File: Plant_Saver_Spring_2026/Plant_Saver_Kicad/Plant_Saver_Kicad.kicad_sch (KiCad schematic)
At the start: 21 parts, among them SW1 Up, SW2 Down, SW3 Change Screen, SW4 Select, U1 TPB4056A20-ES1R, U3 AMS1117-3.3, U5 ESP32-WROOM-32D

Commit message: Added Charging Schematic
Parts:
- added CR2, CR3, CR4: PMEG3050EP_115, SDO_CFP5_SOD128_NEX, symbol PMEG3050EP,115:PMEG3050EP_115
- added SC1, SC2, SC3: Solar_Cell, symbol Device:Solar_Cell
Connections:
- net GND: now also SC1.2 (-), SC2.2 (-), SC3.2 (-)
- new net Power_And_Charging/Solar: CR2.1, CR3.1, CR4.1
- new net Solar_Measurement1/Vin: CR2.2, SC1.1 (+)
- new net Solar_Measurement2/Vin: CR3.2, SC2.1 (+)
- new net Solar_Measurement3/Vin: CR4.2, SC3.1 (+)
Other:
- added sheet Power_And_Charging (Charge_Circuit.kicad_sch)
- added sheet Solar_Measurement1 (Solar_Measurement_Unit.kicad_sch)
- added sheet Solar_Measurement2 (Solar_Measurement_Unit.kicad_sch)
- added sheet Solar_Measurement3 (Solar_Measurement_Unit.kicad_sch)
- added sheet USB-C (USB_C.kicad_sch)
- moved on the sheet: SW1, SW2, SW3, SW4, U5

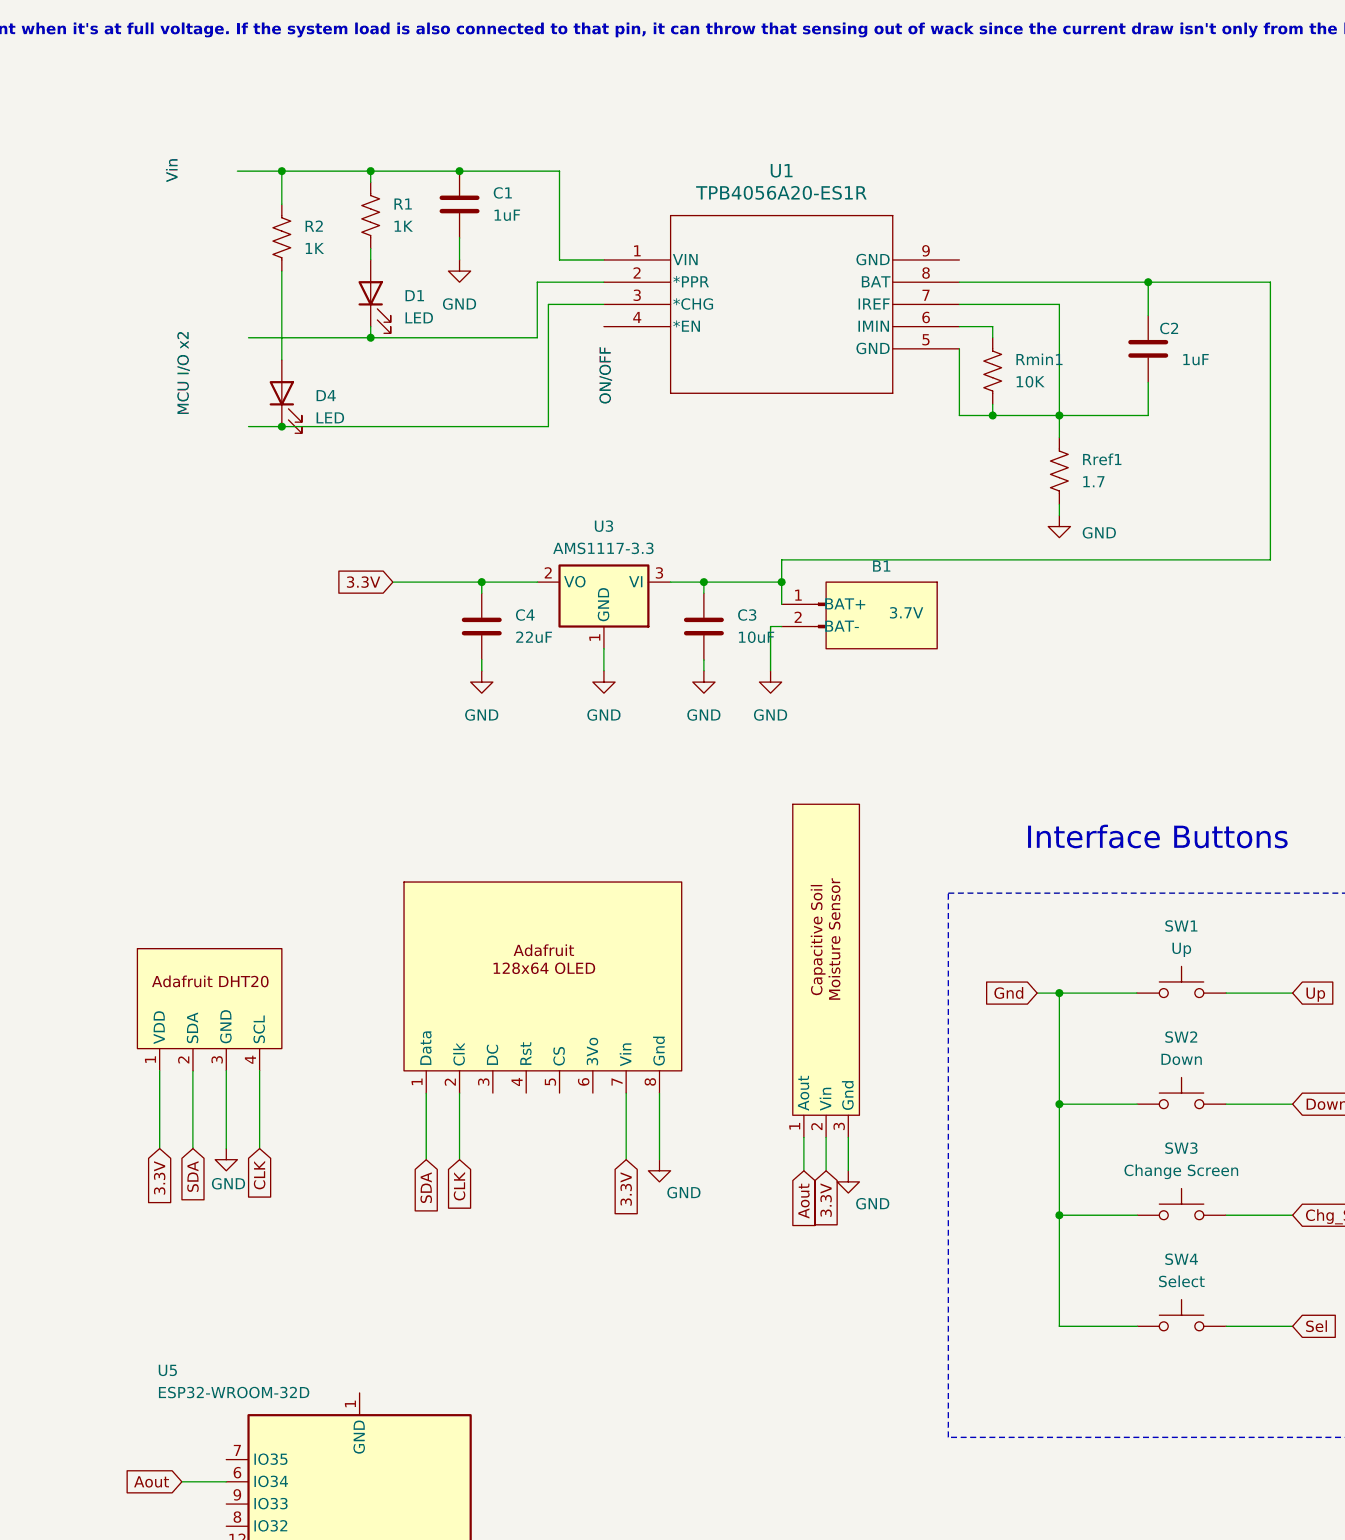
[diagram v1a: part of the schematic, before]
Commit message: Sensor Fun
Had to annotate in order to assign footprints, If that messed anything up I'd be happy to fix it. Added a basic 1x4 header for the temp sensor and added the correct female pins/header footprint for the capacitive moisture sensor. Also put a footprint in there for the OLED using the 4pin cable that we don't have but would be nice to. If we choose to go with the headers instead it's and easy change.
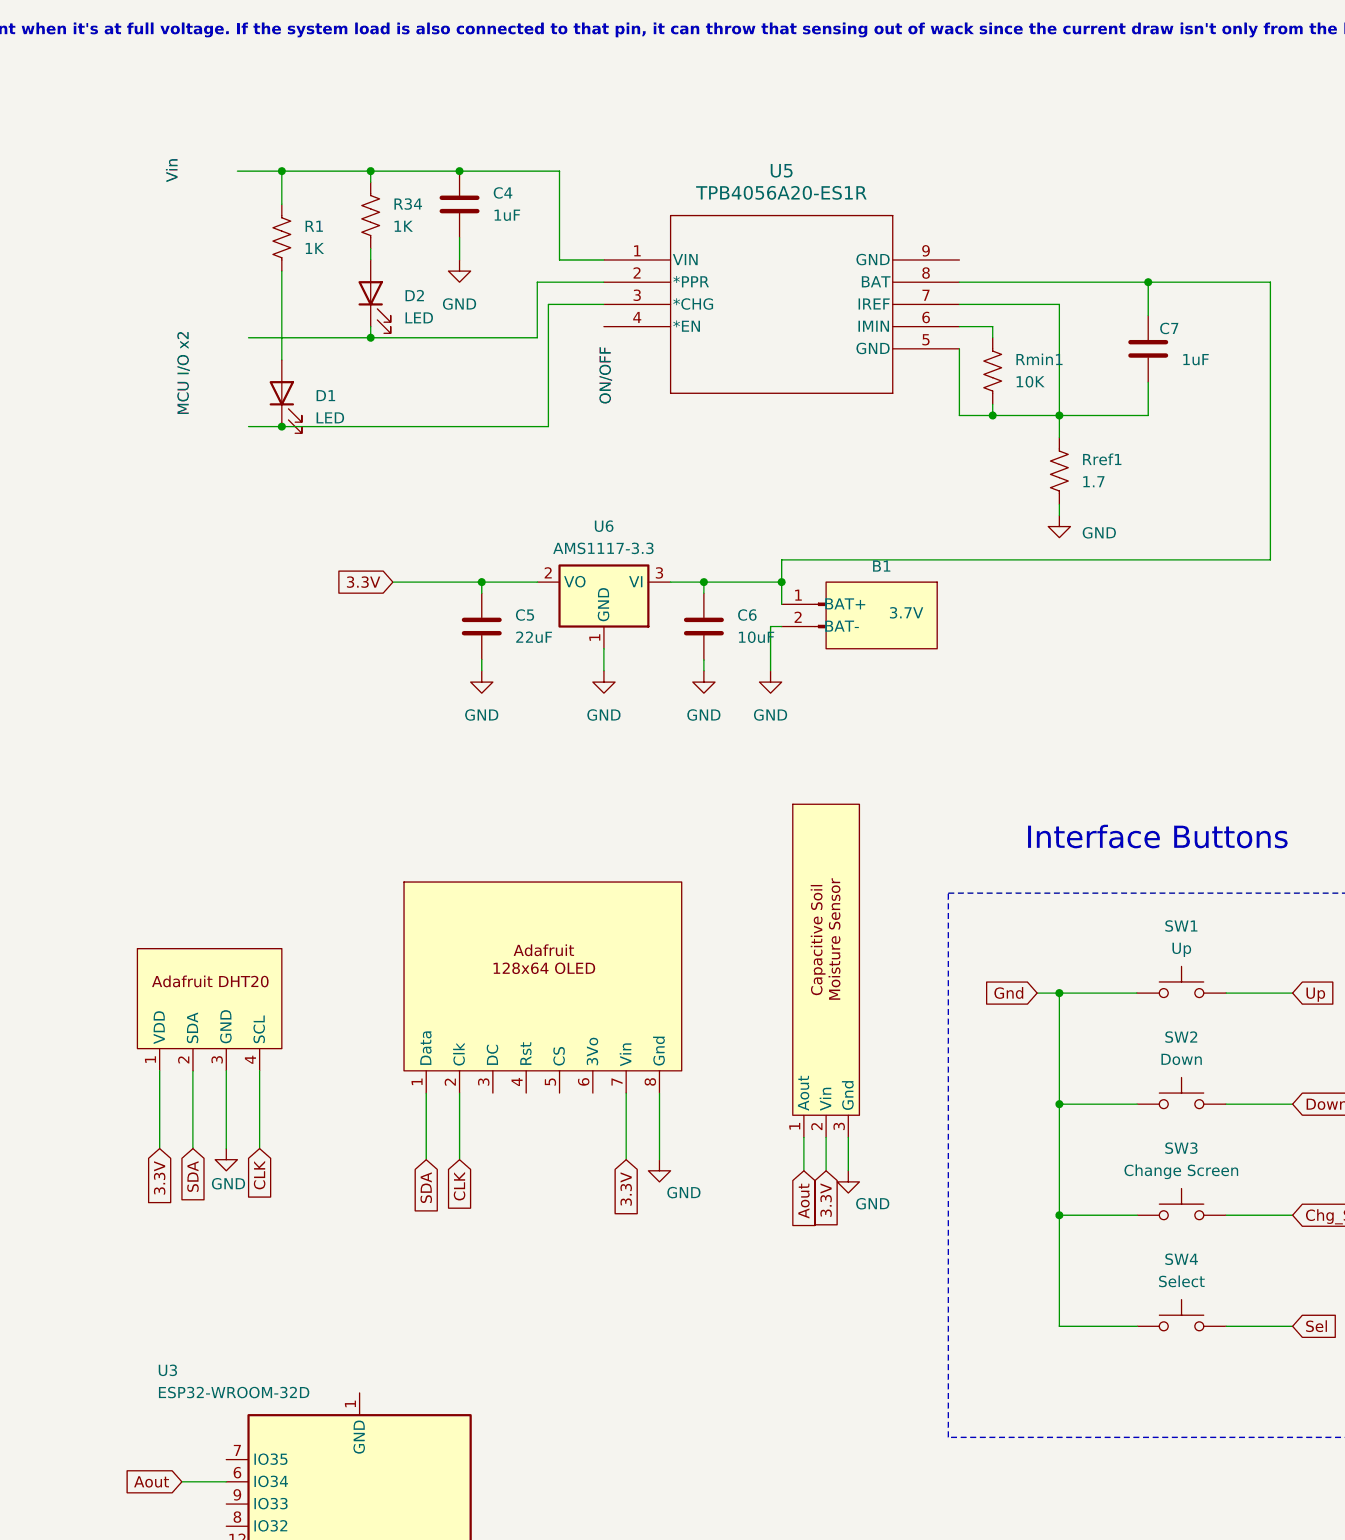
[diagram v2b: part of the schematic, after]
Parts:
- CR2, CR3, CR4: footprint SDO_CFP5_SOD128_NEX -> (none)
- U13: renamed from U4; footprint (none) -> Connector_PinHeader_2.54mm:PinHeader_1x03_P2.54mm_Horizontal
- U2: footprint (none) -> Connector_PinHeader_2.54mm:PinHeader_1x04_P2.54mm_Vertical
- U4: renamed from U6; footprint (none) -> Connector_JST:JST_SH_SM04B-SRSS-TB_1x04-1MP_P1.00mm_Horizontal
- renumbered C1 to C4, C4 to C5, C3 to C6, C2 to C7, D4 to D1, D1 to D2, R2 to R1, R1 to R34, U5 to U3, U1 to U5, U3 to U6
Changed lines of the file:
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@@
 		(on_board yes)
 		(dnp no)
-		(property "Reference" "#PWR09"
+		(property "Reference" "#PWR06"
 			(at 259.08 158.75 0)
 			(effects
@@
 			(project "Plant_Saver_Kicad"
 				(path "/7f244634-d37a-4ff0-ba36-8027330ab1bd"
-					(reference "#PWR09")
+					(reference "#PWR06")
 					(unit 1)
 				)
@@
 			)
 		)
-		(property "Footprint" "SDO_CFP5_SOD128_NEX"
+		(property "Footprint" ""
 			(at 93.98 149.86 0)
 			(effects
@@
 		(dnp no)
 		(fields_autoplaced yes)
-		(property "Reference" "#PWR05"
+		(property "Reference" "#PWR08"
 			(at 288.29 104.14 0)
 			(effects
@@
 			(project "Plant_Saver_Kicad"
 				(path "/7f244634-d37a-4ff0-ba36-8027330ab1bd"
-					(reference "#PWR05")
+					(reference "#PWR08")
 					(unit 1)
 				)
@@
 		(dnp no)
 		(fields_autoplaced yes)
-		(property "Reference" "D1"
+		(property "Reference" "D2"
 			(at 279.4 54.9274 90)
 			(effects
@@
 			(project ""
 				(path "/7f244634-d37a-4ff0-ba36-8027330ab1bd"
-					(reference "D1")
+					(reference "D2")
 					(unit 1)
 				)
@@
 		(on_board yes)
 		(dnp no)
-		(property "Reference" "#PWR08"
+		(property "Reference" "#PWR011"
 			(at 308.61 160.02 0)
 			(effects
@@
 			(project "Plant_Saver_Kicad"
 				(path "/7f244634-d37a-4ff0-ba36-8027330ab1bd"
-					(reference "#PWR08")
+					(reference "#PWR011")
 					(unit 1)
 				)
@@
 			)
 		)
-		(property "Footprint" "SDO_CFP5_SOD128_NEX"
+		(property "Footprint" ""
 			(at 27.94 149.86 0)
 			(effects
@@
 			)
 		)
-		(property "Footprint" "SDO_CFP5_SOD128_NEX"
+		(property "Footprint" ""
 			(at 60.96 149.86 0)
 			(effects
@@
 		(dnp no)
 		(fields_autoplaced yes)
-		(property "Reference" "C1"
+		(property "Reference" "C4"
 			(at 289.56 43.1799 0)
 			(effects
@@
 			(project "Plant_Saver_Kicad"
 				(path "/7f244634-d37a-4ff0-ba36-8027330ab1bd"
-					(reference "C1")
+					(reference "C4")
 					(unit 1)
 				)
@@
 		(dnp no)
 		(fields_autoplaced yes)
-		(property "Reference" "#PWR022"
+		(property "Reference" "#PWR02"
 			(at 59.69 114.3 0)
 			(effects
@@
 			(project "Plant_Saver_Kicad"
 				(path "/7f244634-d37a-4ff0-ba36-8027330ab1bd"
-					(reference "#PWR022")
+					(reference "#PWR02")
 					(unit 1)
 				)
@@
 		(dnp no)
 		(fields_autoplaced yes)
-		(property "Reference" "R1"
+		(property "Reference" "R34"
 			(at 278.13 44.4499 0)
 			(effects
@@
 			(project "Plant_Saver_Kicad"
 				(path "/7f244634-d37a-4ff0-ba36-8027330ab1bd"
-					(reference "R1")
+					(reference "R34")
 					(unit 1)
 				)
@@
 		(on_board yes)
 		(dnp no)
-		(property "Reference" "#PWR04"
+		(property "Reference" "#PWR023"
 			(at 354.33 86.36 0)
 			(effects
@@
 			(project "Plant_Saver_Kicad"
 				(path "/7f244634-d37a-4ff0-ba36-8027330ab1bd"
-					(reference "#PWR04")
+					(reference "#PWR023")
 					(unit 1)
 				)
@@
 		(dnp no)
 		(fields_autoplaced yes)
-		(property "Reference" "#PWR02"
+		(property "Reference" "#PWR09"
 			(at 302.26 104.14 0)
 			(effects
@@
 			(project "Plant_Saver_Kicad"
 				(path "/7f244634-d37a-4ff0-ba36-8027330ab1bd"
-					(reference "#PWR02")
+					(reference "#PWR09")
 					(unit 1)
 				)
@@
 		(dnp no)
 		(fields_autoplaced yes)
-		(property "Reference" "#PWR023"
+		(property "Reference" "#PWR03"
 			(at 91.44 134.62 0)
 			(effects
@@
 			(project "Plant_Saver_Kicad"
 				(path "/7f244634-d37a-4ff0-ba36-8027330ab1bd"
-					(reference "#PWR023")
+					(reference "#PWR03")
 					(unit 1)
 				)
@@
 		(on_board yes)
 		(dnp no)
-		(property "Reference" "U5"
+		(property "Reference" "U3"
 			(at 251.206 177.8 0)
 			(effects
@@
 			(project "Plant_Saver_Kicad"
 				(path "/7f244634-d37a-4ff0-ba36-8027330ab1bd"
-					(reference "U5")
+					(reference "U3")
 					(unit 1)
 				)
@@
 		(dnp no)
 		(fields_autoplaced yes)
-		(property "Reference" "#PWR01"
+		(property "Reference" "#PWR07"
 			(at 285.75 57.15 0)
 			(effects
@@
 			(project "Plant_Saver_Kicad"
 				(path "/7f244634-d37a-4ff0-ba36-8027330ab1bd"
-					(reference "#PWR01")
+					(reference "#PWR07")
 					(unit 1)
 				)
@@
 		(dnp no)
 		(fields_autoplaced yes)
-		(property "Reference" "#PWR07"
+		(property "Reference" "#PWR016"
 			(at 313.69 104.14 0)
 			(effects
@@
 			(project "Plant_Saver_Kicad"
 				(path "/7f244634-d37a-4ff0-ba36-8027330ab1bd"
-					(reference "#PWR07")
+					(reference "#PWR016")
 					(unit 1)
 				)
@@
 		(dnp no)
 		(fields_autoplaced yes)
-		(property "Reference" "R2"
+		(property "Reference" "R1"
 			(at 267.97 46.9899 0)
 			(effects
@@
 			(project "Plant_Saver_Kicad"
 				(path "/7f244634-d37a-4ff0-ba36-8027330ab1bd"
-					(reference "R2")
+					(reference "R1")
 					(unit 1)
 				)
@@
 		(dnp no)
 		(fields_autoplaced yes)
-		(property "Reference" "C3"
+		(property "Reference" "C6"
 			(at 317.5 91.4399 0)
 			(effects
@@
 			(project ""
 				(path "/7f244634-d37a-4ff0-ba36-8027330ab1bd"
-					(reference "C3")
+					(reference "C6")
 					(unit 1)
 				)
@@
 		(on_board yes)
 		(dnp no)
-		(property "Reference" "U3"
+		(property "Reference" "U6"
 			(at 302.26 81.28 0)
 			(effects
@@
 			(project ""
 				(path "/7f244634-d37a-4ff0-ba36-8027330ab1bd"
-					(reference "U3")
+					(reference "U6")
 					(unit 1)
 				)
@@
 		(dnp no)
 		(fields_autoplaced yes)
-		(property "Reference" "U4"
+		(property "Reference" "U13"
 			(at 332.74 129.5399 0)
 			(effects
@@
 			)
 		)
-		(property "Footprint" ""
+		(property "Footprint" "Connector_PinHeader_2.54mm:PinHeader_1x03_P2.54mm_Horizontal"
 			(at 327.66 148.59 0)
 			(effects
@@
 			(project "Plant_Saver_Kicad"
 				(path "/7f244634-d37a-4ff0-ba36-8027330ab1bd"
-					(reference "U4")
+					(reference "U13")
 					(unit 1)
 				)
@@
 		(dnp no)
 		(fields_autoplaced yes)
-		(property "Reference" "D4"
+		(property "Reference" "D1"
 			(at 269.24 66.3574 90)
 			(effects
@@
 			(project ""
 				(path "/7f244634-d37a-4ff0-ba36-8027330ab1bd"
-					(reference "D4")
+					(reference "D1")
 					(unit 1)
 				)
@@
 		(dnp no)
 		(fields_autoplaced yes)
-		(property "Reference" "U1"
+		(property "Reference" "U5"
 			(at 322.58 40.64 0)
 			(effects
@@
 			(project "Plant_Saver_Kicad"
 				(path "/7f244634-d37a-4ff0-ba36-8027330ab1bd"
-					(reference "U1")
+					(reference "U5")
 					(unit 1)
 				)
@@
 			)
 		)
-		(property "Footprint" ""
+		(property "Footprint" "Connector_PinHeader_2.54mm:PinHeader_1x04_P2.54mm_Vertical"
 			(at 257.81 134.62 0)
 			(effects
@@
 		(dnp no)
 		(fields_autoplaced yes)
-		(property "Reference" "#PWR03"
+		(property "Reference" "#PWR021"
 			(at 321.31 104.14 0)
 			(effects
@@
 			(project ""
 				(path "/7f244634-d37a-4ff0-ba36-8027330ab1bd"
-					(reference "#PWR03")
+					(reference "#PWR021")
 					(unit 1)
 				)
@@
 		(on_board yes)
 		(dnp no)
-		(property "Reference" "#PWR06"
+		(property "Reference" "#PWR022"
 			(at 330.2 161.29 0)
 			(effects
@@
 			(project "Plant_Saver_Kicad"
 				(path "/7f244634-d37a-4ff0-ba36-8027330ab1bd"
-					(reference "#PWR06")
+					(reference "#PWR022")
 					(unit 1)
 				)
@@
 		(on_board yes)
 		(dnp no)
-		(property "Reference" "C2"
+		(property "Reference" "C7"
 			(at 365.76 58.674 0)
 			(effects
@@
 			(project "Plant_Saver_Kicad"
 				(path "/7f244634-d37a-4ff0-ba36-8027330ab1bd"
-					(reference "C2")
+					(reference "C7")
 					(unit 1)
 				)
@@
 		(dnp no)
 		(fields_autoplaced yes)
-		(property "Reference" "#PWR011"
+		(property "Reference" "#PWR05"
 			(at 139.7 161.29 0)
 			(effects
@@
 			(project ""
 				(path "/7f244634-d37a-4ff0-ba36-8027330ab1bd"
-					(reference "#PWR011")
+					(reference "#PWR05")
 					(unit 1)
 				)
@@
 		(dnp no)
 		(fields_autoplaced yes)
-		(property "Reference" "U6"
+		(property "Reference" "U4"
 			(at 312.42 131.4449 0)
 			(effects
@@
 			)
 		)
-		(property "Footprint" ""
+		(property "Footprint" "Connector_JST:JST_SH_SM04B-SRSS-TB_1x04-1MP_P1.00mm_Horizontal"
 			(at 294.64 133.35 0)
 			(effects
@@
 			(project "Plant_Saver_Kicad"
 				(path "/7f244634-d37a-4ff0-ba36-8027330ab1bd"
-					(reference "U6")
+					(reference "U4")
 					(unit 1)
 				)
@@
 		(dnp no)
 		(fields_autoplaced yes)
-		(property "Reference" "#PWR021"
+		(property "Reference" "#PWR01"
 			(at 27.94 93.98 0)
 			(effects
@@
 			(project "Plant_Saver_Kicad"
 				(path "/7f244634-d37a-4ff0-ba36-8027330ab1bd"
-					(reference "#PWR021")
+					(reference "#PWR01")
 					(unit 1)
 				)
@@
 		(dnp no)
 		(fields_autoplaced yes)
-		(property "Reference" "#PWR016"
+		(property "Reference" "#PWR04"
 			(at 93.98 187.96 0)
 			(effects
@@
 			(project "Plant_Saver_Kicad"
 				(path "/7f244634-d37a-4ff0-ba36-8027330ab1bd"
-					(reference "#PWR016")
+					(reference "#PWR04")
 					(unit 1)
 				)
@@
 		(dnp no)
 		(fields_autoplaced yes)
-		(property "Reference" "C4"
+		(property "Reference" "C5"
 			(at 292.1 91.4399 0)
 			(effects
@@
 			(project ""
 				(path "/7f244634-d37a-4ff0-ba36-8027330ab1bd"
-					(reference "C4")
-					(unit 1)
-				)
+					(reference "C5")
+					(unit 1)
+				)
